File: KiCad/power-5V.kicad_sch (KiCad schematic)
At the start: 7 parts, among them U1 TPSM63606RDLR

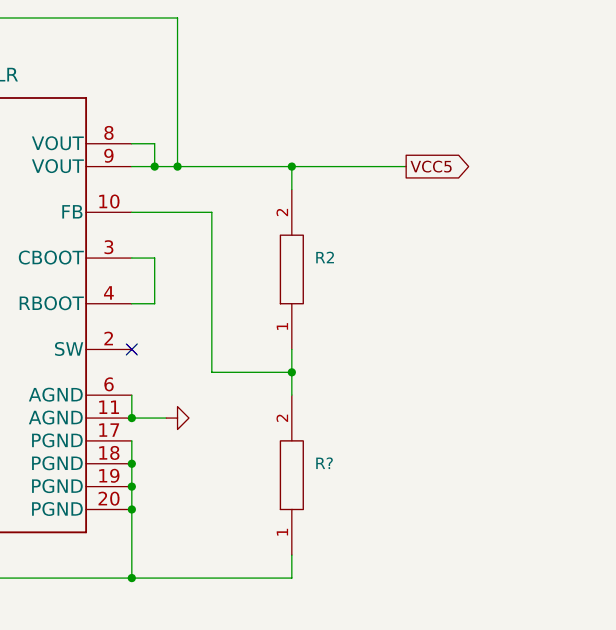
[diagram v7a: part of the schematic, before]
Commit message: feat(pcb): add feedback capacitor
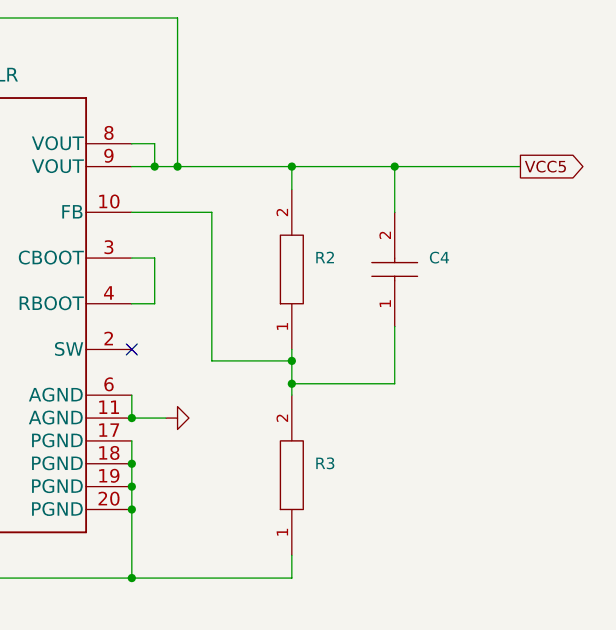
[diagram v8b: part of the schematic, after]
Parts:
- added C4: (no value), symbol GRM1555C1H8R2CA01D:GRM1555C1H8R2CA01D
- gave numbers to parts that had none: 1
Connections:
- net VCC5: now also C4.2
- net at R2.1, R3.2, U1.10 (FB): now also C4.1
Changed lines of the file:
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@@
   (junction (at 128.27 129.54) (diameter 0) (color 0 0 0 0)
   )
-  (junction (at 195.58 106.68) (diameter 0) (color 0 0 0 0)
-  )
   (junction (at 177.8 129.54) (diameter 0) (color 0 0 0 0)
   )
+  (junction (at 195.58 105.41) (diameter 0) (color 0 0 0 0)
+  )
   (junction (at 177.8 119.38) (diameter 0) (color 0 0 0 0)
   )
   (junction (at 180.34 83.82) (diameter 0) (color 0 0 0 0)
   )
+  (junction (at 195.58 107.95) (diameter 0) (color 0 0 0 0)
+  )
   (junction (at 127 83.82) (diameter 0) (color 0 0 0 0)
+  )
+  (junction (at 207.01 83.82) (diameter 0) (color 0 0 0 0)
   )
   (junction (at 104.14 101.6) (diameter 0) (color 0 0 0 0)
@@
     (stroke (width 0) (type default) (color 0 0 0 0))
   )
-  (wire (pts (xy 195.58 83.82) (xy 208.28 83.82))
+  (wire (pts (xy 195.58 83.82) (xy 207.01 83.82))
     (stroke (width 0) (type default) (color 0 0 0 0))
   )
@@
     (stroke (width 0) (type default) (color 0 0 0 0))
   )
+  (wire (pts (xy 207.01 107.95) (xy 195.58 107.95))
+    (stroke (width 0) (type default) (color 0 0 0 0))
+  )
   (wire (pts (xy 129.54 67.31) (xy 182.88 67.31))
     (stroke (width 0) (type default) (color 0 0 0 0))
@@
     (stroke (width 0) (type default) (color 0 0 0 0))
   )
-  (wire (pts (xy 186.69 88.9) (xy 186.69 106.68))
+  (wire (pts (xy 186.69 88.9) (xy 186.69 105.41))
     (stroke (width 0) (type default) (color 0 0 0 0))
   )
@@
     (stroke (width 0) (type default) (color 0 0 0 0))
   )
-  (wire (pts (xy 186.69 106.68) (xy 195.58 106.68))
+  (wire (pts (xy 186.69 105.41) (xy 195.58 105.41))
+    (stroke (width 0) (type default) (color 0 0 0 0))
+  )
+  (wire (pts (xy 207.01 101.6) (xy 207.01 107.95))
     (stroke (width 0) (type default) (color 0 0 0 0))
   )
@@
     (stroke (width 0) (type default) (color 0 0 0 0))
   )
+  (wire (pts (xy 207.01 83.82) (xy 207.01 88.9))
+    (stroke (width 0) (type default) (color 0 0 0 0))
+  )
   (wire (pts (xy 116.84 83.82) (xy 116.84 86.36))
     (stroke (width 0) (type default) (color 0 0 0 0))
@@
     (stroke (width 0) (type default) (color 0 0 0 0))
   )
+  (wire (pts (xy 195.58 105.41) (xy 195.58 107.95))
+    (stroke (width 0) (type default) (color 0 0 0 0))
+  )
   (wire (pts (xy 177.8 119.38) (xy 177.8 121.92))
     (stroke (width 0) (type default) (color 0 0 0 0))
@@
     (stroke (width 0) (type default) (color 0 0 0 0))
   )
-  (wire (pts (xy 195.58 104.14) (xy 195.58 106.68))
+  (wire (pts (xy 195.58 104.14) (xy 195.58 105.41))
     (stroke (width 0) (type default) (color 0 0 0 0))
   )
@@
     (stroke (width 0) (type default) (color 0 0 0 0))
   )
+  (wire (pts (xy 207.01 83.82) (xy 220.98 83.82))
+    (stroke (width 0) (type default) (color 0 0 0 0))
+  )
   (wire (pts (xy 180.34 99.06) (xy 177.8 99.06))
     (stroke (width 0) (type default) (color 0 0 0 0))
   )
-  (wire (pts (xy 195.58 106.68) (xy 195.58 109.22))
-    (stroke (width 0) (type default) (color 0 0 0 0))
-  )
   (wire (pts (xy 104.14 129.54) (xy 104.14 130.81))
     (stroke (width 0) (type default) (color 0 0 0 0))
@@
     (stroke (width 0) (type default) (color 0 0 0 0))
   )
+  (wire (pts (xy 195.58 107.95) (xy 195.58 109.22))
+    (stroke (width 0) (type default) (color 0 0 0 0))
+  )
   (wire (pts (xy 116.84 99.06) (xy 116.84 101.6))
     (stroke (width 0) (type default) (color 0 0 0 0))
@@
     (stroke (width 0) (type default) (color 0 0 0 0))
   )
-  (global_label "VCC5" (shape output) (at 208.28 83.82 0) (fields_autoplaced)
+  (global_label "VCC5" (shape output) (at 220.98 83.82 0) (fields_autoplaced)
     (effects (font (size 1.27 1.27)) (justify left))
-    (property "Intersheet References" "${INTERSHEET_REFS}" (id 0) (at 215.5312 83.7406 0)
+    (property "Intersheet References" "${INTERSHEET_REFS}" (id 0) (at 228.2312 83.7406 0)
       (effects (font (size 1.27 1.27)) (justify left) hide)
     )
@@
   (symbol (lib_id "CRCW040210K0FKED:CRCW040210K0FKED") (at 195.58 127 90) (unit 1)
     (in_bom yes) (on_board yes) (fields_autoplaced)
-    (property "Reference" "R?" (id 0) (at 198.12 116.8399 90)
+    (property "Reference" "R3" (id 0) (at 198.12 116.8399 90)
       (effects (font (size 1.27 1.27)) (justify right))
     )
@@
       (effects (font (size 1.27 1.27)) (justify left) hide)
     )
+    (pin "1")
+    (pin "2")
+  )
+  (symbol (lib_id "GRM1555C1H8R2CA01D:GRM1555C1H8R2CA01D") (at 207.01 101.6 90) (unit 1)
+    (in_bom yes) (on_board yes) (fields_autoplaced)
+    (property "Reference" "C4" (id 0) (at 210.82 93.9799 90)
+      (effects (font (size 1.27 1.27)) (justify right))
+    )
+    (property "Value" "" (id 1) (at 210.82 96.5199 90)
+      (effects (font (size 1.27 1.27)) (justify right))
+    )
+    (property "Footprint" "" (id 2) (at 205.74 92.71 0)
+      (effects (font (size 1.27 1.27)) (justify left) hide)
+    )
+    (property "Datasheet" "https://datasheet.datasheetarchive.com/originals/distributors/Datasheets_SAMA/ec4f1577dddcc7a13ddad897a28002d3.pdf" (id 3) (at 208.28 92.71 0)
+      (effects (font (size 1.27 1.27)) (justify left) hide)
+    )
+    (property "Description" "MURATA - GRM1555C1H8R2CA01D - CAP, MLCC, C0G/NP0, 8.2PF, 50V, 0402" (id 4) (at 210.82 92.71 0)
+      (effects (font (size 1.27 1.27)) (justify left) hide)
+    )
+    (property "Height" "0.55" (id 5) (at 213.36 92.71 0)
+      (effects (font (size 1.27 1.27)) (justify left) hide)
+    )
+    (property "Mouser Part Number" "81-GRM1555C1H8R2CA1D" (id 6) (at 215.9 92.71 0)
+      (effects (font (size 1.27 1.27)) (justify left) hide)
+    )
+    (property "Mouser Price/Stock" "https://www.mouser.co.uk/ProductDetail/Murata-Electronics/GRM1555C1H8R2CA01D?qs=q312vENifzBDSINEH9AUSg%3D%3D" (id 7) (at 218.44 92.71 0)
+      (effects (font (size 1.27 1.27)) (justify left) hide)
+    )
+    (property "Manufacturer_Name" "Murata Electronics" (id 8) (at 220.98 92.71 0)
+      (effects (font (size 1.27 1.27)) (justify left) hide)
+    )
+    (property "Manufacturer_Part_Number" "GRM1555C1H8R2CA01D" (id 9) (at 223.52 92.71 0)
+      (effects (font (size 1.27 1.27)) (justify left) hide)
+    )
